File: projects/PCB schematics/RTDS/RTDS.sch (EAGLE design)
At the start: 0 parts

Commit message: RTDS - Intial commit.
Board not in draft state yet. Committing out to add in parts to master.
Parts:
- added U$1: NANO, Arduino-clone:NANO
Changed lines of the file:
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@@
 <setting verticaltext="up"/>
 </settings>
-<grid distance="0.1" unitdist="inch" unit="inch" style="lines" multiple="1" display="no" altdistance="0.01" altunitdist="inch" altunit="inch"/>
+<grid distance="0.1" unitdist="inch" unit="inch" style="lines" multiple="1" display="yes" altdistance="0.01" altunitdist="inch" altunit="inch"/>
 <layers>
+<layer number="1" name="Top" color="4" fill="1" visible="no" active="no"/>
+<layer number="16" name="Bottom" color="1" fill="1" visible="no" active="no"/>
+<layer number="17" name="Pads" color="2" fill="1" visible="no" active="no"/>
+<layer number="18" name="Vias" color="2" fill="1" visible="no" active="no"/>
+<layer number="19" name="Unrouted" color="6" fill="1" visible="no" active="no"/>
+<layer number="20" name="Dimension" color="15" fill="1" visible="no" active="no"/>
+<layer number="21" name="tPlace" color="7" fill="1" visible="no" active="no"/>
+<layer number="22" name="bPlace" color="7" fill="1" visible="no" active="no"/>
+<layer number="23" name="tOrigins" color="15" fill="1" visible="no" active="no"/>
+<layer number="24" name="bOrigins" color="15" fill="1" visible="no" active="no"/>
+<layer number="25" name="tNames" color="7" fill="1" visible="no" active="no"/>
+<layer number="26" name="bNames" color="7" fill="1" visible="no" active="no"/>
+<layer number="27" name="tValues" color="7" fill="1" visible="no" active="no"/>
+<layer number="28" name="bValues" color="7" fill="1" visible="no" active="no"/>
+<layer number="29" name="tStop" color="7" fill="3" visible="no" active="no"/>
+<layer number="30" name="bStop" color="7" fill="6" visible="no" active="no"/>
+<layer number="31" name="tCream" color="7" fill="4" visible="no" active="no"/>
+<layer number="32" name="bCream" color="7" fill="5" visible="no" active="no"/>
+<layer number="33" name="tFinish" color="6" fill="3" visible="no" active="no"/>
+<layer number="34" name="bFinish" color="6" fill="6" visible="no" active="no"/>
+<layer number="35" name="tGlue" color="7" fill="4" visible="no" active="no"/>
+<layer number="36" name="bGlue" color="7" fill="5" visible="no" active="no"/>
+<layer number="37" name="tTest" color="7" fill="1" visible="no" active="no"/>
+<layer number="38" name="bTest" color="7" fill="1" visible="no" active="no"/>
+<layer number="39" name="tKeepout" color="4" fill="11" visible="no" active="no"/>
+<layer number="40" name="bKeepout" color="1" fill="11" visible="no" active="no"/>
+<layer number="41" name="tRestrict" color="4" fill="10" visible="no" active="no"/>
+<layer number="42" name="bRestrict" color="1" fill="10" visible="no" active="no"/>
+<layer number="43" name="vRestrict" color="2" fill="10" visible="no" active="no"/>
+<layer number="44" name="Drills" color="7" fill="1" visible="no" active="no"/>
+<layer number="45" name="Holes" color="7" fill="1" visible="no" active="no"/>
+<layer number="46" name="Milling" color="3" fill="1" visible="no" active="no"/>
+<layer number="47" name="Measures" color="7" fill="1" visible="no" active="no"/>
+<layer number="48" name="Document" color="7" fill="1" visible="no" active="no"/>
+<layer number="49" name="Reference" color="7" fill="1" visible="no" active="no"/>
+<layer number="51" name="tDocu" color="7" fill="1" visible="no" active="no"/>
+<layer number="52" name="bDocu" color="7" fill="1" visible="no" active="no"/>
 <layer number="88" name="SimResults" color="9" fill="1" visible="yes" active="yes"/>
 <layer number="89" name="SimProbes" color="9" fill="1" visible="yes" active="yes"/>
@@
 </classes>
 <parts>
+<part name="U$1" library="Arduino-clone" deviceset="NANO" device=""/>
 </parts>
 <sheets>
@@
 </plain>
 <instances>
+<instance part="U$1" gate="G$1" x="40.64" y="43.18" smashed="yes"/>
 </instances>
 <busses>

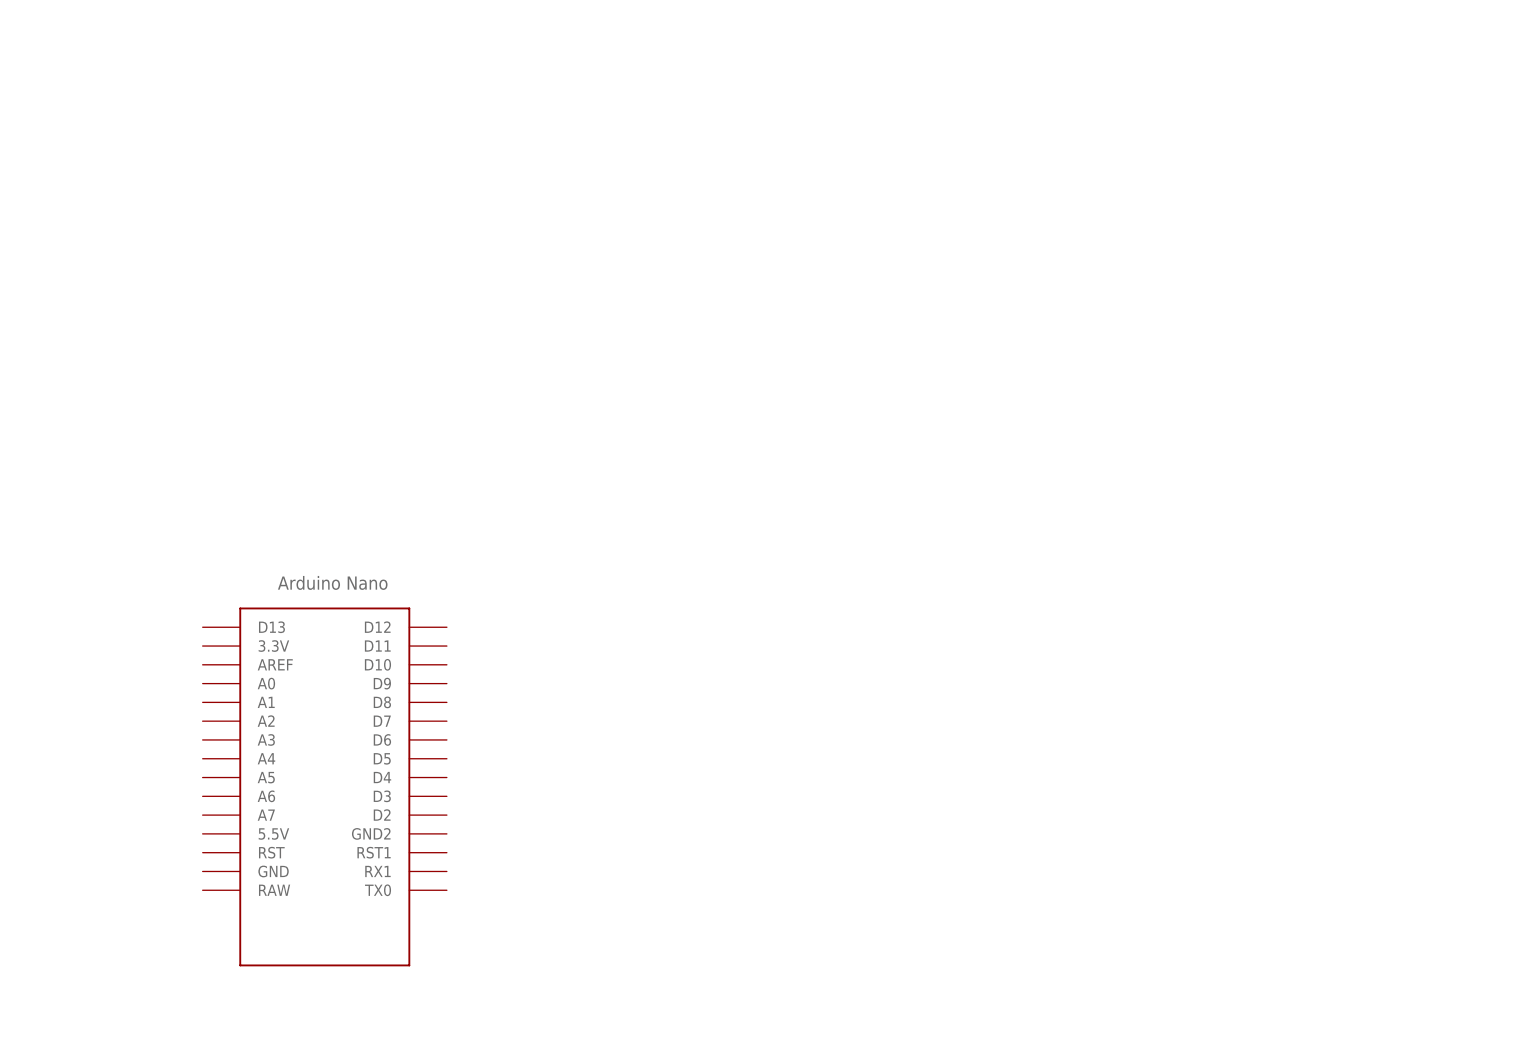
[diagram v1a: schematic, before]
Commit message: RTDS - Initial draft.
Arduino Nano and SoundFX boards added.
Must complete wiring.
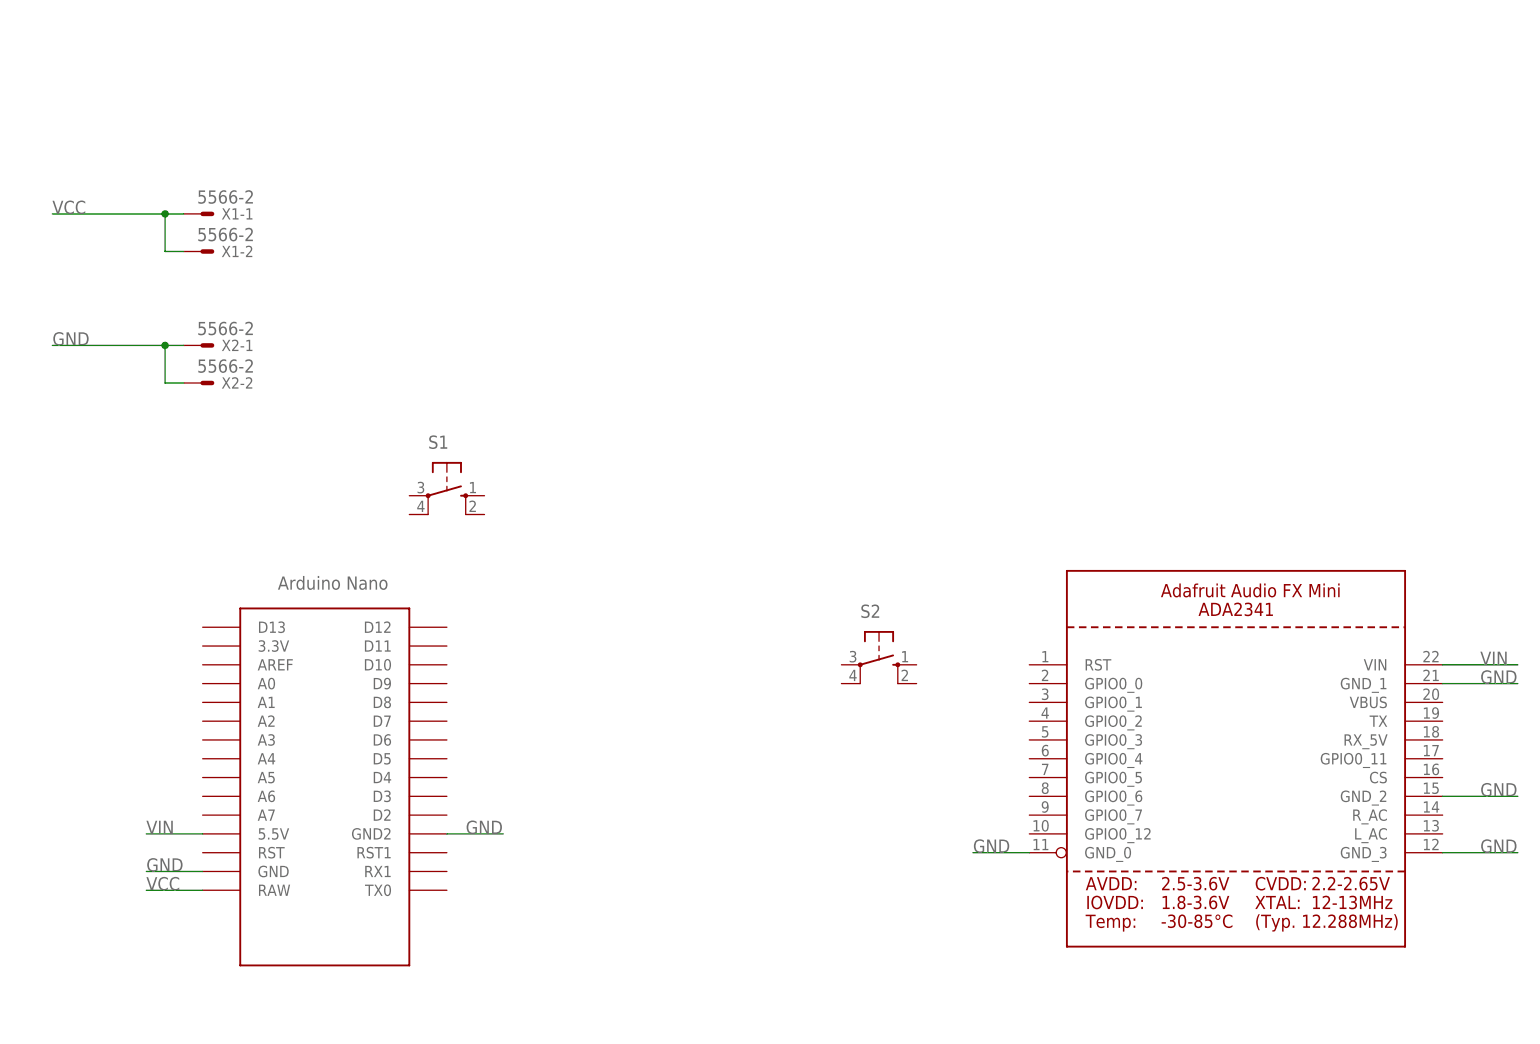
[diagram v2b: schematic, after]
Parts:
- added S1, S2: (no value), switch-omron:10-XX
- added U$2: ADA-SOUNDFX, IowaFormula:ADA-SOUNDFX
- added X1, X2: 5566-2, con-molex:5566-2
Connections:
- new net GND: U$1.GND, U$1.GND2, U$2.GND_0, U$2.GND_1, U$2.GND_2, U$2.GND_3, X2-1.S, X2-2.S
- new net VCC: U$1.RAW, X1-1.S, X1-2.S
- new net VIN: U$1.5.5V, U$2.VIN

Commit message: RTDS - Rev A.
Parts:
- removed S1, S2: (no value), switch-omron:10-XX
- added R1, R2: 47k, rcl:R-US_R0805
- added SH1: SHORTT5, shorts:SHORTT5
- added U$3: MAX9744, IowaFormula:MAX9744
- added X3, X4, X5: 5566-2, con-molex:5566-2
- U$1: value NANO -> MAX9744; device Arduino-clone:NANO -> IowaFormula:MAX9744
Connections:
- new net +12V-ISO: X1-1.S, X1-2.S, X2-1.S, X2-2.S
- new net AUDIO_GND: U$1.AGND, U$2.GND_3, U$3.AGND
- new net LEFT: U$2.L_AC
- new net N$1: U$1.GND
- new net RESET_SIGNAL: R2.2, U$2.RST
- new net RIGHT: U$2.R_AC
- new net RTDS_SIGNAL: R1.2, U$2.GPIO0_0, X5-1.S, X5-2.S
- net GND: now also U$3.GND, X4-1.S, X4-2.S; no longer U$1.GND, U$1.GND2, U$2.GND_3, X2-1.S, X2-2.S
- net VCC: now also R1.1, R2.1, SH1.P$2, X3-1.S, X3-2.S; no longer U$1.RAW, X1-1.S, X1-2.S
- net VIN: now also SH1.P$1; no longer U$1.5.5V
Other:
- moved on the sheet: X1-1, X1-2, X2-1, X2-2

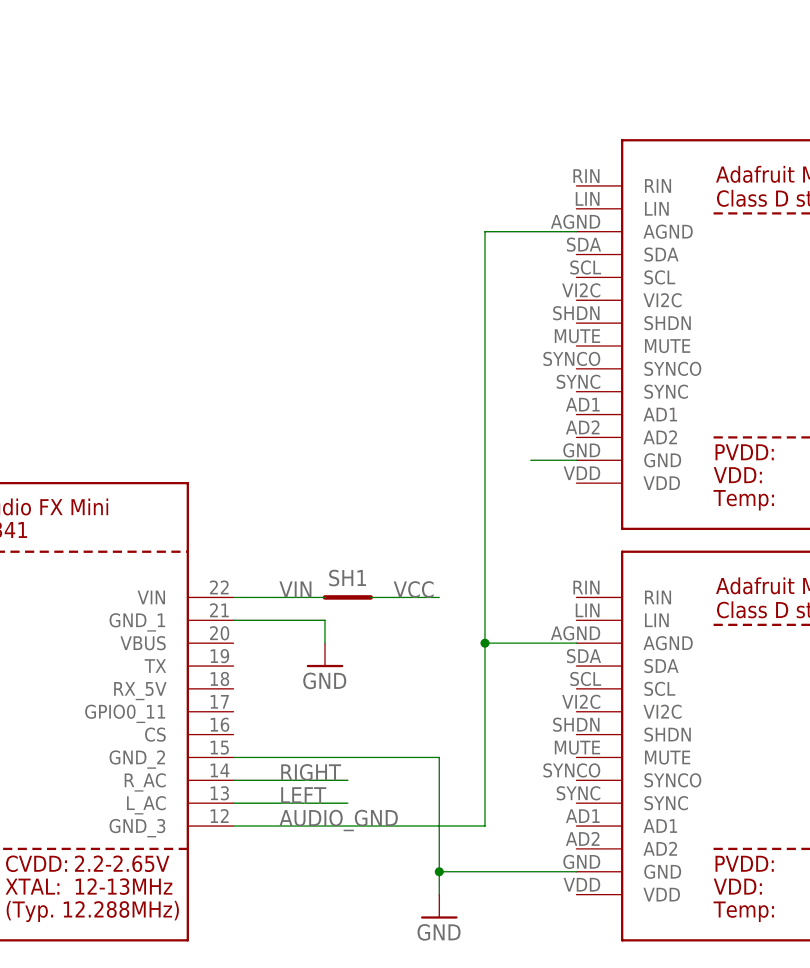
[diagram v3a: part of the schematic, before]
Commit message: RTDS - R L audio wiring to amplifiers.
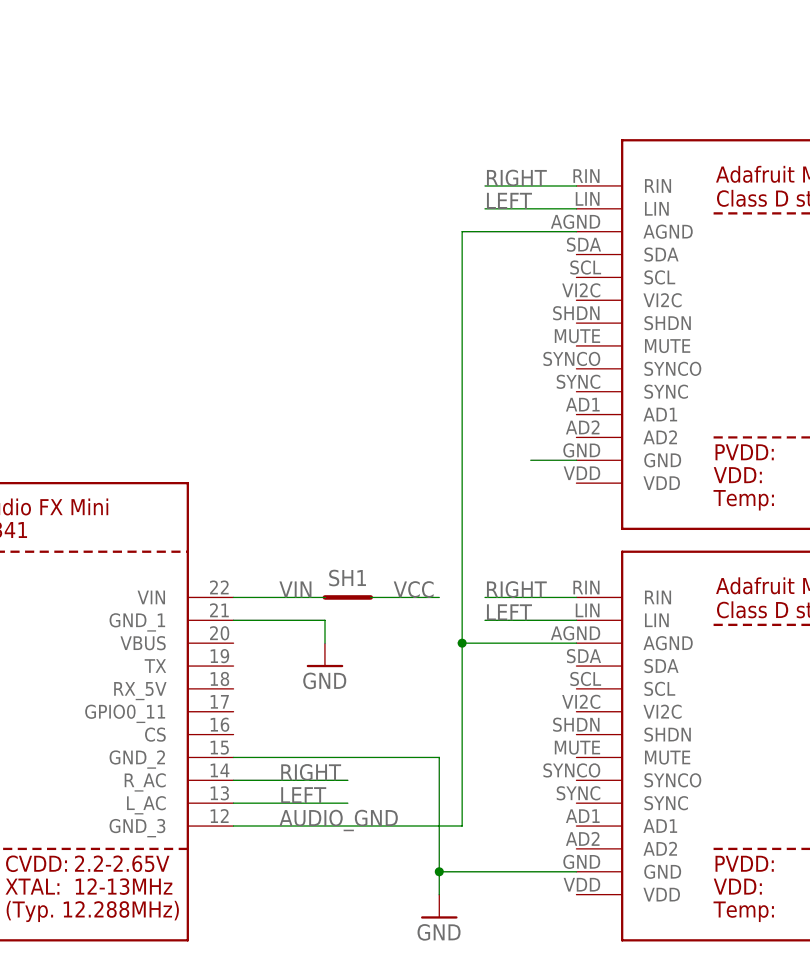
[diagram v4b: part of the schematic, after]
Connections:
- net LEFT: now also U$1.LIN, U$3.LIN
- net RIGHT: now also U$1.RIN, U$3.RIN
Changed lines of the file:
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@@
 <label x="106.68" y="22.86" size="1.778" layer="95"/>
+</segment>
+<segment>
+<pinref part="U$1" gate="A" pin="RIN"/>
+<wire x1="139.7" y1="88.9" x2="129.54" y2="88.9" width="0.1524" layer="91"/>
+<label x="129.54" y="88.9" size="1.778" layer="95"/>
+</segment>
+<segment>
+<wire x1="139.7" y1="43.18" x2="129.54" y2="43.18" width="0.1524" layer="91"/>
+<label x="129.54" y="43.18" size="1.778" layer="95"/>
+<pinref part="U$3" gate="A" pin="RIN"/>
 </segment>
 </net>
@@
 <label x="106.68" y="20.32" size="1.778" layer="95"/>
 </segment>
+<segment>
+<pinref part="U$1" gate="A" pin="LIN"/>
+<wire x1="139.7" y1="86.36" x2="129.54" y2="86.36" width="0.1524" layer="91"/>
+<label x="129.54" y="86.36" size="1.778" layer="95"/>
+</segment>
+<segment>
+<wire x1="139.7" y1="40.64" x2="129.54" y2="40.64" width="0.1524" layer="91"/>
+<label x="129.54" y="40.64" size="1.778" layer="95"/>
+<pinref part="U$3" gate="A" pin="LIN"/>
+</segment>
 </net>
 <net name="AUDIO_GND" class="0">
@@
 <label x="106.68" y="17.78" size="1.778" layer="95"/>
 <pinref part="U$2" gate="A" pin="GND_3"/>
-<wire x1="101.6" y1="17.78" x2="129.54" y2="17.78" width="0.1524" layer="91"/>
-<wire x1="129.54" y1="17.78" x2="129.54" y2="38.1" width="0.1524" layer="91"/>
+<wire x1="101.6" y1="17.78" x2="127" y2="17.78" width="0.1524" layer="91"/>
+<wire x1="127" y1="17.78" x2="127" y2="38.1" width="0.1524" layer="91"/>
 <pinref part="U$3" gate="A" pin="AGND"/>
-<wire x1="129.54" y1="38.1" x2="139.7" y2="38.1" width="0.1524" layer="91"/>
+<wire x1="127" y1="38.1" x2="139.7" y2="38.1" width="0.1524" layer="91"/>
 <pinref part="U$1" gate="A" pin="AGND"/>
-<wire x1="129.54" y1="38.1" x2="129.54" y2="83.82" width="0.1524" layer="91"/>
-<wire x1="129.54" y1="83.82" x2="139.7" y2="83.82" width="0.1524" layer="91"/>
-<junction x="129.54" y="38.1"/>
+<wire x1="127" y1="38.1" x2="127" y2="83.82" width="0.1524" layer="91"/>
+<wire x1="127" y1="83.82" x2="139.7" y2="83.82" width="0.1524" layer="91"/>
+<junction x="127" y="38.1"/>
 </segment>
 </net>
